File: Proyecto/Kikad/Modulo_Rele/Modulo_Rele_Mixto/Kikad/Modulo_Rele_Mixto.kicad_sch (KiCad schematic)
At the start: 9 parts, among them J1 TB_1X3, J2 TB_1X3, K1 RELAY_C, Q1 BC337, U3 PC817

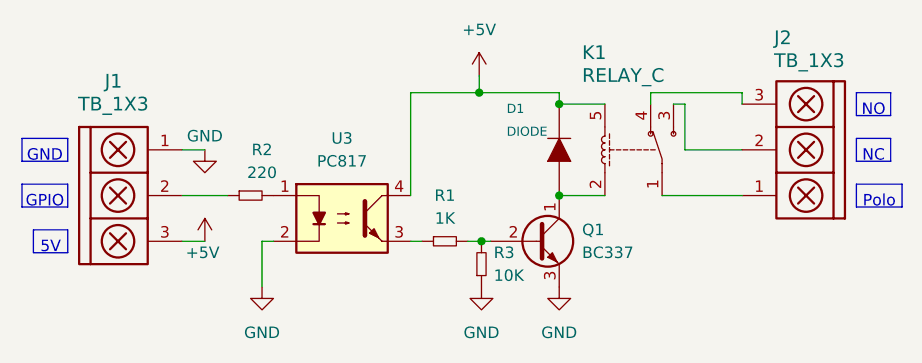
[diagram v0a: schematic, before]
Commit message: hice el Rele Mixto y adjunte sus imagenes. ademas agregue la resistencia de 10K
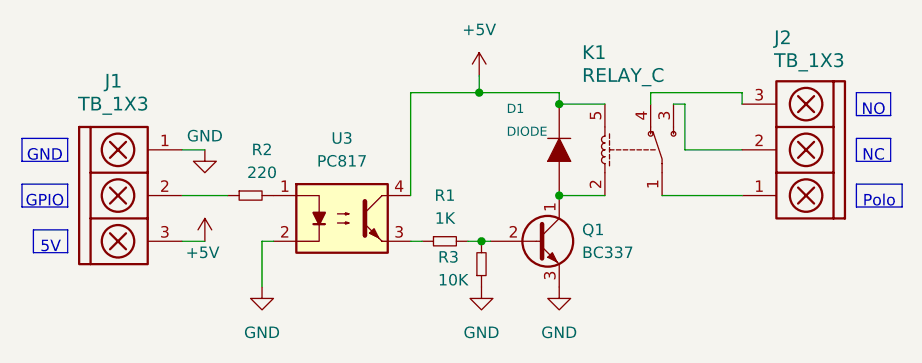
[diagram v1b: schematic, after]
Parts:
- D1: footprint Diode_THT:D_A-405_P7.62mm_Horizontal -> Diode_SMD:D_SMA
- R1, R2, R3: footprint Resistor_THT:R_Axial_DIN0207_L6.3mm_D2.5mm_P10.16mm_Horizontal -> Diode_SMD:D_0805_2012Metric
- U3: footprint Package_DIP:DIP-4_W7.62mm -> Package_SO:SSO-4_6.7x5.1mm_P2.54mm_Clearance8mm

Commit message: Agregue la carpeta Placa_Principal e hice unas correcciones en el Modulo_Rele
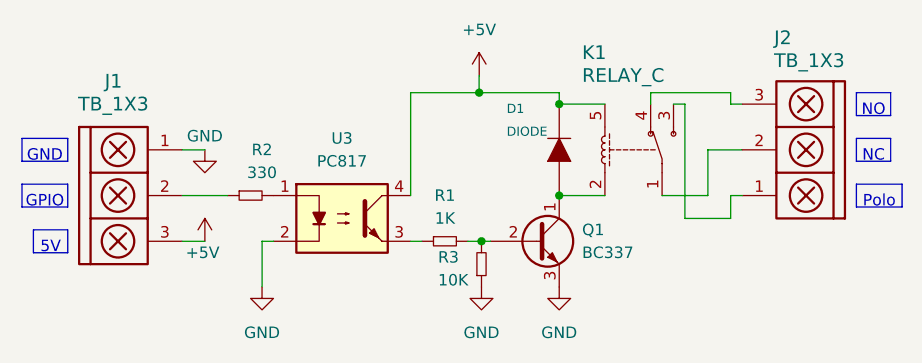
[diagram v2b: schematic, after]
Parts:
- J1: footprint Connector_Molex:Molex_KK-254_AE-6410-03A_1x03_P2.54mm_Vertical -> Connector_PinHeader_2.54mm:PinHeader_1x03_P2.54mm_Vertical
- J2: footprint Connector_Molex:Molex_KK-254_AE-6410-03A_1x03_P2.54mm_Vertical -> TerminalBlock:TerminalBlock_bornier-3_P5.08mm
- R2: value 220 -> 330
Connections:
- net at J2.1: now also K1.3; no longer K1.1
- net at J2.2: now also K1.1; no longer K1.3
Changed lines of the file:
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@@
 	(wire
 		(pts
-			(xy 160.02 73.66) (xy 168.91 73.66)
+			(xy 160.02 73.66) (xy 165.1 73.66)
 		)
 		(stroke
@@
 	(wire
 		(pts
-			(xy 158.75 62.23) (xy 168.91 62.23)
+			(xy 162.56 76.2) (xy 167.64 76.2)
+		)
+		(stroke
+			(width 0)
+			(type default)
+		)
+	)
+	(wire
+		(pts
+			(xy 158.75 62.23) (xy 167.64 62.23)
 		)
 		(stroke
@@
 	(wire
 		(pts
+			(xy 165.1 73.66) (xy 165.1 68.58)
+		)
+		(stroke
+			(width 0)
+			(type default)
+		)
+	)
+	(wire
+		(pts
 			(xy 132.08 78.74) (xy 133.35 78.74)
 		)
@@
 	(wire
 		(pts
-			(xy 162.56 63.5) (xy 162.56 68.58)
-		)
-		(stroke
-			(width 0)
-			(type default)
-		)
-	)
-	(wire
-		(pts
-			(xy 162.56 68.58) (xy 168.91 68.58)
-		)
-		(stroke
-			(width 0)
-			(type default)
-		)
-	)
-	(wire
-		(pts
-			(xy 168.91 62.23) (xy 168.91 63.5)
+			(xy 167.64 63.5) (xy 168.91 63.5)
+		)
+		(stroke
+			(width 0)
+			(type default)
+		)
+	)
+	(wire
+		(pts
+			(xy 167.64 62.23) (xy 167.64 63.5)
+		)
+		(stroke
+			(width 0)
+			(type default)
+		)
+	)
+	(wire
+		(pts
+			(xy 167.64 73.66) (xy 168.91 73.66)
 		)
 		(stroke
@@
 	(wire
 		(pts
+			(xy 162.56 63.5) (xy 162.56 76.2)
+		)
+		(stroke
+			(width 0)
+			(type default)
+		)
+	)
+	(wire
+		(pts
 			(xy 158.75 63.5) (xy 158.75 62.23)
 		)
@@
 	(wire
 		(pts
+			(xy 167.64 76.2) (xy 167.64 73.66)
+		)
+		(stroke
+			(width 0)
+			(type default)
+		)
+	)
+	(wire
+		(pts
 			(xy 148.59 62.23) (xy 148.59 63.5)
+		)
+		(stroke
+			(width 0)
+			(type default)
+		)
+	)
+	(wire
+		(pts
+			(xy 165.1 68.58) (xy 168.91 68.58)
 		)
 		(stroke
@@
 			)
 		)
-		(property "Footprint" "Connector_Molex:Molex_KK-254_AE-6410-03A_1x03_P2.54mm_Vertical"
+		(property "Footprint" "Connector_PinHeader_2.54mm:PinHeader_1x03_P2.54mm_Vertical"
 			(at 96.52 69.85 0)
 			(effects
@@
 			)
 		)
-		(property "Footprint" "Connector_Molex:Molex_KK-254_AE-6410-03A_1x03_P2.54mm_Vertical"
+		(property "Footprint" "TerminalBlock:TerminalBlock_bornier-3_P5.08mm"
 			(at 185.42 54.102 0)
 			(effects
@@
 			)
 		)
-		(property "Value" "220"
+		(property "Value" "330"
 			(at 115.57 71.12 90)
 			(effects
